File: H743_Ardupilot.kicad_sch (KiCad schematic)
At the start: 8 parts, among them U1 Power_Protection:USBLC6-2P6

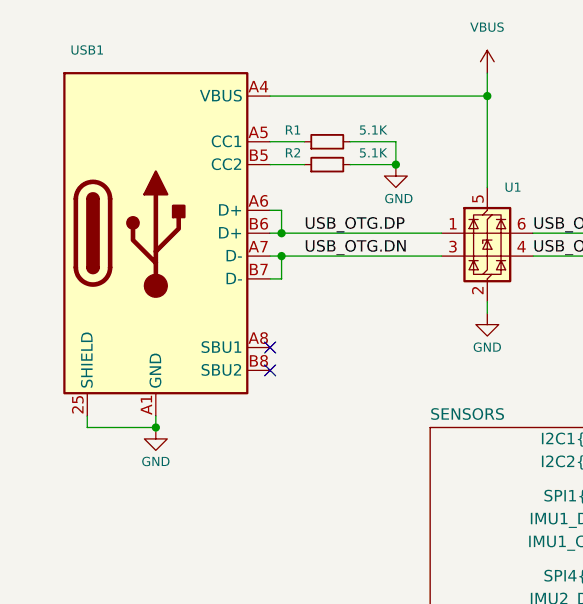
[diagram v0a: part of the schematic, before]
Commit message: Update USB1 DX07S016JA1R1500 schematic and DigiKey data
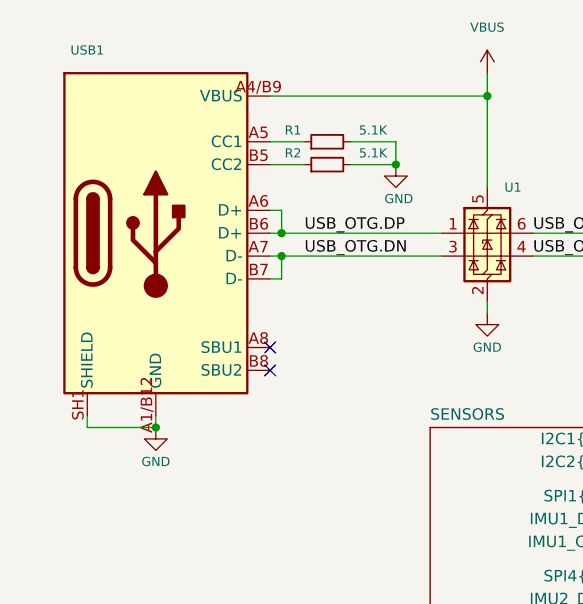
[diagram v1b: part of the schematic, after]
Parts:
- USB1: value USB_C_Receptacle_USB2.0_16P -> DX07S016JA1R1500; DigiKey Part Number (none) -> 670-DX07S016JA1R1500TR-ND; DigiKey Price Qty (none) -> 1500 (Tape & Reel); DigiKey Unit Price EUR (none) -> 0.86782; JAE Drawing (none) -> SJ121836 / SJ121837; Price Checked (none) -> 2026-09-27; Supplier PDF (none) -> https://mm.digikey.com/Volume0/opasdata/d220001/medias/docu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; Supplier Specs (none) -> 16 pos.; USB 2.0 Type-C; 5 A max; 48 Vrms; -40..+85 C; 1000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
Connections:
- net GND: now also USB1.A1/B12 (GND), USB1.A12/B1 (GND), USB1.SH1 (SHIELD), USB1.SH2 (SHIELD), USB1.SH3 (SHIELD), USB1.SH4 (SHIELD), USB1.SH5 (SHIELD), USB1.SH6 (SHIELD); no longer USB1.25 (SHIELD), USB1.26 (SHIELD), USB1.27 (SHIELD), USB1.28 (SHIELD), USB1.A1 (GND), USB1.A12 (GND), USB1.B1 (GND), USB1.B12 (GND)
- net VBUS: now also USB1.A4/B9 (VBUS), USB1.B4/A9 (VBUS); no longer USB1.A4 (VBUS), USB1.A9 (VBUS), USB1.B4 (VBUS), USB1.B9 (VBUS)
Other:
- moved on the sheet: USB1
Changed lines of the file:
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@@
 			)
 		)
-		(property "Value" "USB_C_Receptacle_USB2.0_16P"
+		(property "Value" "DX07S016JA1R1500"
 			(at 53.34 35.56 0)
 			(hide yes)
@@
 			)
 		)
-		(property "Datasheet" "https://www.jae.com/en/connectors/series/detail/product/id=91780"
-			(at 53.34 55.88 0)
-			(hide yes)
-			(show_name no)
-			(do_not_autoplace no)
-			(effects
-				(font
-					(size 1.27 1.27)
-				)
-			)
-		)
-		(property "Description" "USB Type-C receptacle, USB 2.0, 16 positions, right-angle on-board SMT, JAE DX07S016JA1R1500"
+		(property "Datasheet" "https://mm.digikey.com/Volume0/opasdata/d220001/medias/docus/7162/670_DX07S016JA1R1500.pdf"
+			(at 53.34 55.88 0)
+			(hide yes)
+			(show_name no)
+			(do_not_autoplace no)
+			(effects
+				(font
+					(size 1.27 1.27)
+				)
+			)
+		)
+		(property "Description" "JAE DX07S016JA1R1500; USB Type-C USB 2.0 receptacle; 16 positions (24 = 16+8 dummy per DigiKey); on-board/right-angle, 1-row SMT + shell through-hole; shell DIP 0.9 mm; 5 A max; 48 Vrms; -40..+85 C; 10000 mating cycles. Supplier PDF: https://mm.digikey.com/Volume0/opasdata/d220001/medias/docus/7162/670_DX07S016JA1R1500.pdf"
 			(at 53.34 55.88 0)
 			(hide yes)
@@
 			)
 		)
+		(property "DigiKey Part Number" "670-DX07S016JA1R1500TR-ND"
+			(at 53.34 55.88 0)
+			(hide yes)
+			(show_name no)
+			(do_not_autoplace no)
+			(effects
+				(font
+					(size 1 1)
+					(thickness 0.15)
+				)
+			)
+		)
 		(property "Manufacturer" "JAE Electronics"
 			(at 53.34 55.88 0)
@@
 			)
 		)
+		(property "DigiKey Unit Price EUR" "0.86782"
+			(at 53.34 55.88 0)
+			(hide yes)
+			(show_name no)
+			(do_not_autoplace no)
+			(effects
+				(font
+					(size 1 1)
+					(thickness 0.15)
+				)
+			)
+		)
+		(property "DigiKey Price Qty" "1500 (Tape & Reel)"
+			(at 53.34 55.88 0)
+			(hide yes)
+			(show_name no)
+			(do_not_autoplace no)
+			(effects
+				(font
+					(size 1 1)
+					(thickness 0.15)
+				)
+			)
+		)
+		(property "Price Checked" "2026-09-27"
+			(at 53.34 55.88 0)
+			(hide yes)
+			(show_name no)
+			(do_not_autoplace no)
+			(effects
+				(font
+					(size 1 1)
+					(thickness 0.15)
+				)
+			)
+		)
+		(property "Supplier PDF" "https://mm.digikey.com/Volume0/opasdata/d220001/medias/docus/7162/670_DX07S016JA1R1500.pdf"
+			(at 53.34 55.88 0)
+			(hide yes)
+			(show_name no)
+			(do_not_autoplace no)
+			(effects
+				(font
+					(size 1 1)
+					(thickness 0.15)
+				)
+			)
+		)
+		(property "JAE Drawing" "SJ121836 / SJ121837"
+			(at 53.34 55.88 0)
+			(hide yes)
+			(show_name no)
+			(do_not_autoplace no)
+			(effects
+				(font
+					(size 1 1)
+					(thickness 0.15)
+				)
+			)
+		)
+		(property "Supplier Specs" "16 pos.; USB 2.0 Type-C; 5 A max; 48 Vrms; -40..+85 C; 10000 cycles; shell DIP 0.9 mm; 1500 pcs/reel"
+			(at 53.34 55.88 0)
+			(hide yes)
+			(show_name no)
+			(do_not_autoplace no)
+			(effects
+				(font
+					(size 1 1)
+					(thickness 0.15)
+				)
+			)
+		)
 		(property "Mouser URL" "https://www.mouser.com/ProductDetail/JAE-Electronics/DX07S016JA1R1500"
 			(at 53.34 55.88 0)
@@
 			)
 		)
-		(pin "B12"
-		)
-		(pin "B9"
-		)
 		(pin "B8"
 		)
@@
 		(pin "B6"
 		)
-		(pin "A1"
-		)
-		(pin "27"
-		)
-		(pin "26"
-		)
-		(pin "28"
-		)
-		(pin "A4"
-		)
-		(pin "25"
+		(pin "A1/B12"
+		)
+		(pin "SH3"
+		)
+		(pin "SH2"
+		)
+		(pin "SH4"
+		)
+		(pin "SH5"
+		)
+		(pin "SH6"
+		)
+		(pin "A4/B9"
+		)
+		(pin "SH1"
 		)
 		(pin "A5"
@@
 		(pin "B5"
 		)
-		(pin "A12"
-		)
-		(pin "B4"
+		(pin "A12/B1"
+		)
+		(pin "B4/A9"
 		)
 		(pin "A8"
 		)
-		(pin "B1"
-		)
-		(pin "A9"
-		)
 		(instances

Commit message: Update USB1 ESD protection footprint and package
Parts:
- U1: value Power_Protection:USBLC6-2P6 -> USBLC6-2P6; footprint Package_TO_SOT_SMD:SOT-666 -> H743_Custom:ST_USBLC6-2P6_SOT-666; Associated Connector (none) -> USB1 (DX07S016JA1R1500); DigiKey Part Number (none) -> 497-5026-1-ND; DigiKey Price Qty (none) -> 1 (Cut Tape); DigiKey URL (none) -> https://www.digikey.fr/fr/products/detail/stmicroelectronic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; DigiKey Unit Price EUR (none) -> 0.56000; MPN (none) -> USBLC6-2P6; Manufacturer (none) -> STMicroelectronics; Package (none) -> SOT-666, 1.6 x 1.6 x 0.55 mm; Price Checked (none) -> 2026-09-27; Supplier PDF (none) -> https://www.st.com/resource/en/datasheet/usblc6-2.pdf
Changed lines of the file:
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@@
 			)
 		)
-		(property "Value" "Power_Protection:USBLC6-2P6"
+		(property "Value" "USBLC6-2P6"
 			(at 91.8211 50.8 0)
 			(hide yes)
@@
 			)
 		)
-		(property "Footprint" "Package_TO_SOT_SMD:SOT-666"
+		(property "Footprint" "H743_Custom:ST_USBLC6-2P6_SOT-666"
 			(at 91.186 62.611 0)
 			(hide yes)
@@
 			)
 		)
-		(property "Datasheet" "https://www.st.com/resource/en/datasheet/cd00050750.pdf"
+		(property "Datasheet" "https://www.st.com/resource/en/datasheet/usblc6-2.pdf"
 			(at 91.186 64.516 0)
 			(hide yes)
@@
 			)
 		)
-		(property "Description" "Very low capacitance ESD protection diode, 2 data-line, SOT-666"
+		(property "Description" "STMicroelectronics USBLC6-2P6; ESD protection for USB 2.0 high-speed D+/D- and VBUS; SOT-666, 1.6 x 1.6 x 0.55 mm. Used on USB1. Supplier PDF: https://www.st.com/resource/en/datasheet/usblc6-2.pdf"
 			(at 90.17 55.88 0)
 			(hide yes)
@@
 			)
 		)
-		(property "MPN" ""
+		(property "MPN" "USBLC6-2P6"
 			(at 90.17 55.88 0)
 			(hide yes)
@@
 			)
 		)
-		(property "Manufacturer" ""
+		(property "Manufacturer" "STMicroelectronics"
 			(at 90.17 55.88 0)
 			(hide yes)
@@
 				)
 			)
+		)
+		(property "Package" "SOT-666, 1.6 x 1.6 x 0.55 mm"
+			(at 90.17 55.88 0)
+			(hide yes)
+			(show_name no)
+			(do_not_autoplace no)
+			(effects
+				(font
+					(size 1 1)
+					(thickness 0.15)
+				)
+			)
+		)
+		(property "DigiKey Part Number" "497-5026-1-ND"
+			(at 90.17 55.88 0)
+			(hide yes)
+			(show_name no)
+			(do_not_autoplace no)
+			(effects
+				(font
+					(size 1 1)
+					(thickness 0.15)
+				)
+			)
+		)
+		(property "DigiKey URL" "https://www.digikey.fr/fr/products/detail/stmicroelectronics/USBLC6-2P6/1007440"
+			(at 90.17 55.88 0)
+			(hide yes)
+			(show_name no)
+			(do_not_autoplace no)
+			(effects
+				(font
+					(size 1 1)
+					(thickness 0.15)
+				)
+			)
+		)
+		(property "DigiKey Unit Price EUR" "0.56000"
+			(at 90.17 55.88 0)
+			(hide yes)
+			(show_name no)
+			(do_not_autoplace no)
+			(effects
+				(font
+					(size 1 1)
+					(thickness 0.15)
+				)
+			)
+		)
+		(property "DigiKey Price Qty" "1 (Cut Tape)"
+			(at 90.17 55.88 0)
+			(hide yes)
+			(show_name no)
+			(do_not_autoplace no)
+			(effects
+				(font
+					(size 1 1)
+					(thickness 0.15)
+				)
+			)
+		)
+		(property "Price Checked" "2026-09-27"
+			(at 90.17 55.88 0)
+			(hide yes)
+			(show_name no)
+			(do_not_autoplace no)
+			(effects
+				(font
+					(size 1 1)
+					(thickness 0.15)
+				)
+			)
+		)
+		(property "Supplier PDF" "https://www.st.com/resource/en/datasheet/usblc6-2.pdf"
+			(at 90.17 55.88 0)
+			(hide yes)
+			(show_name no)
+			(do_not_autoplace no)
+			(effects
+				(font
+					(size 1 1)
+					(thickness 0.15)
+				)
+			)
+		)
+		(property "Associated Connector" "USB1 (DX07S016JA1R1500)"
+			(at 90.17 55.88 0)
+			(hide yes)
+			(show_name no)
+			(do_not_autoplace no)
+			(effects
+				(font
+					(size 1 1)
+					(thickness 0.15)
+				)
+			)

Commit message: Point U1 to exact SOT50P160X60-6N footprint
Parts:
- U1: footprint H743_Custom:ST_USBLC6-2P6_SOT-666 -> H743_Custom:SOT50P160X60-6N
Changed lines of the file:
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@@
 			)
 		)
-		(property "Footprint" "H743_Custom:ST_USBLC6-2P6_SOT-666"
+		(property "Footprint" "H743_Custom:SOT50P160X60-6N"
 			(at 91.186 62.611 0)
 			(hide yes)

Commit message: Use dedicated USBLC6_2P6 footprint library for U1
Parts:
- U1: footprint H743_Custom:SOT50P160X60-6N -> USBLC6_2P6:SOT50P160X60-6N
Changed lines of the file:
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@@
 			)
 		)
-		(property "Footprint" "H743_Custom:SOT50P160X60-6N"
+		(property "Footprint" "USBLC6_2P6:SOT50P160X60-6N"
 			(at 91.186 62.611 0)
 			(hide yes)

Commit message: Review component footprints, restore local libraries and reconcile PCB pads
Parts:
- H1, H2, H3, H4: symbol Mechanical:MountingHole_Pad -> FC01_Project:H743_Ardupilot__MountingHole_Pad
- R1, R2: symbol Device:R_Small -> FC01_Project:H743_Ardupilot__R_Small
- U1: symbol Power_Protection:USBLC6-2P6 -> FC01_Project:H743_Ardupilot__USBLC6-2P6
- USB1: symbol H743_Ardupilot:USB_C_Receptacle_USB2.0_16P_JAE_DX07S016JA1R1500 -> FC01_Project:H743_Ardupilot__USB_C_Receptacle_USB2.0_16P_JAE_DX07S016JA1R1500; Footprint Audit OK: JAE DX07S016JA1R1500 mechanical geometry; A/B signal pa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 -> See verification/COMPONENTS.csv and verification/REPORT.md; Library Audit Project-local H743_Custom footprint; no EasyEDA footprint d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 -> See verification/COMPONENTS.csv and verification/REPORT.md
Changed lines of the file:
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@@
 	)
 	(symbol
-		(lib_id "power:GND")
+		(lib_id "FC01_Project:H743_Ardupilot__GND")
 		(at 144.78 165.1 0)
 		(unit 1)
@@
 	)
 	(symbol
-		(lib_id "power:VBUS")
+		(lib_id "FC01_Project:H743_Ardupilot__VBUS")
 		(at 90.17 38.1 0)
 		(unit 1)
@@
 	)
 	(symbol
-		(lib_id "power:GND")
+		(lib_id "FC01_Project:H743_Ardupilot__GND")
 		(at 53.34 77.47 0)
 		(unit 1)
@@
 	)
 	(symbol
-		(lib_id "power:GND")
+		(lib_id "FC01_Project:H743_Ardupilot__GND")
 		(at 80.01 48.26 0)
 		(unit 1)
@@
 	)
 	(symbol
-		(lib_id "Device:R_Small")
+		(lib_id "FC01_Project:H743_Ardupilot__R_Small")
 		(at 72.39 45.72 90)
 		(unit 1)
@@
 	)
 	(symbol
-		(lib_id "Device:R_Small")
+		(lib_id "FC01_Project:H743_Ardupilot__R_Small")
 		(at 72.39 48.26 90)
 		(unit 1)
@@
 	)
 	(symbol
-		(lib_id "Mechanical:MountingHole_Pad")
+		(lib_id "FC01_Project:H743_Ardupilot__MountingHole_Pad")
 		(at 137.16 161.29 0)
 		(unit 1)
@@
 	)
 	(symbol
-		(lib_id "power:GND")
+		(lib_id "FC01_Project:H743_Ardupilot__GND")
 		(at 129.54 165.1 0)
 		(unit 1)
@@
 	)
 	(symbol
-		(lib_id "power:GND")
+		(lib_id "FC01_Project:H743_Ardupilot__GND")
 		(at 90.17 64.77 0)
 		(unit 1)
@@
 	)
 	(symbol
-		(lib_id "power:GND")
+		(lib_id "FC01_Project:H743_Ardupilot__GND")
 		(at 137.16 165.1 0)
 		(unit 1)
@@
 	)
 	(symbol
-		(lib_id "Mechanical:MountingHole_Pad")
+		(lib_id "FC01_Project:H743_Ardupilot__MountingHole_Pad")
 		(at 129.54 161.29 0)
 		(unit 1)
@@
 	)
 	(symbol
-		(lib_id "Mechanical:MountingHole_Pad")
+		(lib_id "FC01_Project:H743_Ardupilot__MountingHole_Pad")
 		(at 144.78 161.29 0)
 		(unit 1)
@@
 	)
 	(symbol
-		(lib_id "H743_Ardupilot:USB_C_Receptacle_USB2.0_16P_JAE_DX07S016JA1R1500")
+		(lib_id "FC01_Project:H743_Ardupilot__USB_C_Receptacle_USB2.0_16P_JAE_DX07S016JA1R1500")
 		(at 53.34 55.88 0)
 		(unit 1)
@@
 			)
 		)
-		(property "Footprint Audit" "OK: JAE DX07S016JA1R1500 mechanical geometry; A/B signal pad numbers preserved; four shell pads mapped to symbol pins 25-28"
-			(at 53.34 55.88 0)
-			(hide yes)
-			(show_name no)
-			(do_not_autoplace no)
-			(effects
-				(font
-					(size 1.27 1.27)
-				)
-			)
-		)
-		(property "Library Audit" "Project-local H743_Custom footprint; no EasyEDA footprint dependency"
+		(property "Footprint Audit" "See verification/COMPONENTS.csv and verification/REPORT.md"
+			(at 53.34 55.88 0)
+			(hide yes)
+			(show_name no)
+			(do_not_autoplace no)
+			(effects
+				(font
+					(size 1.27 1.27)
+				)
+			)
+		)
+		(property "Library Audit" "See verification/COMPONENTS.csv and verification/REPORT.md"
 			(at 53.34 55.88 0)
 			(hide yes)
@@
 	)
 	(symbol
-		(lib_id "power:GND")
+		(lib_id "FC01_Project:H743_Ardupilot__GND")
 		(at 152.4 165.1 0)
 		(unit 1)
@@
 	)
 	(symbol
-		(lib_id "Mechanical:MountingHole_Pad")
+		(lib_id "FC01_Project:H743_Ardupilot__MountingHole_Pad")
 		(at 152.4 161.29 0)
 		(unit 1)
@@
 	)
 	(symbol
-		(lib_id "Power_Protection:USBLC6-2P6")
+		(lib_id "FC01_Project:H743_Ardupilot__USBLC6-2P6")
 		(at 90.17 55.88 0)
 		(unit 1)
